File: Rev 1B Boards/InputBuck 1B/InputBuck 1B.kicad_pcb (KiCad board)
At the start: 4 copper layers, 67.2 x 46 mm, 44 parts, among them J1 Conn_01x02_Socket, J16 Banana 2P, J17 Banana 2P, J23 Conn_01x01_Pin, Q1 BSC059N04LS6, Q2 BSC059N04LS6, U1 BQ24640

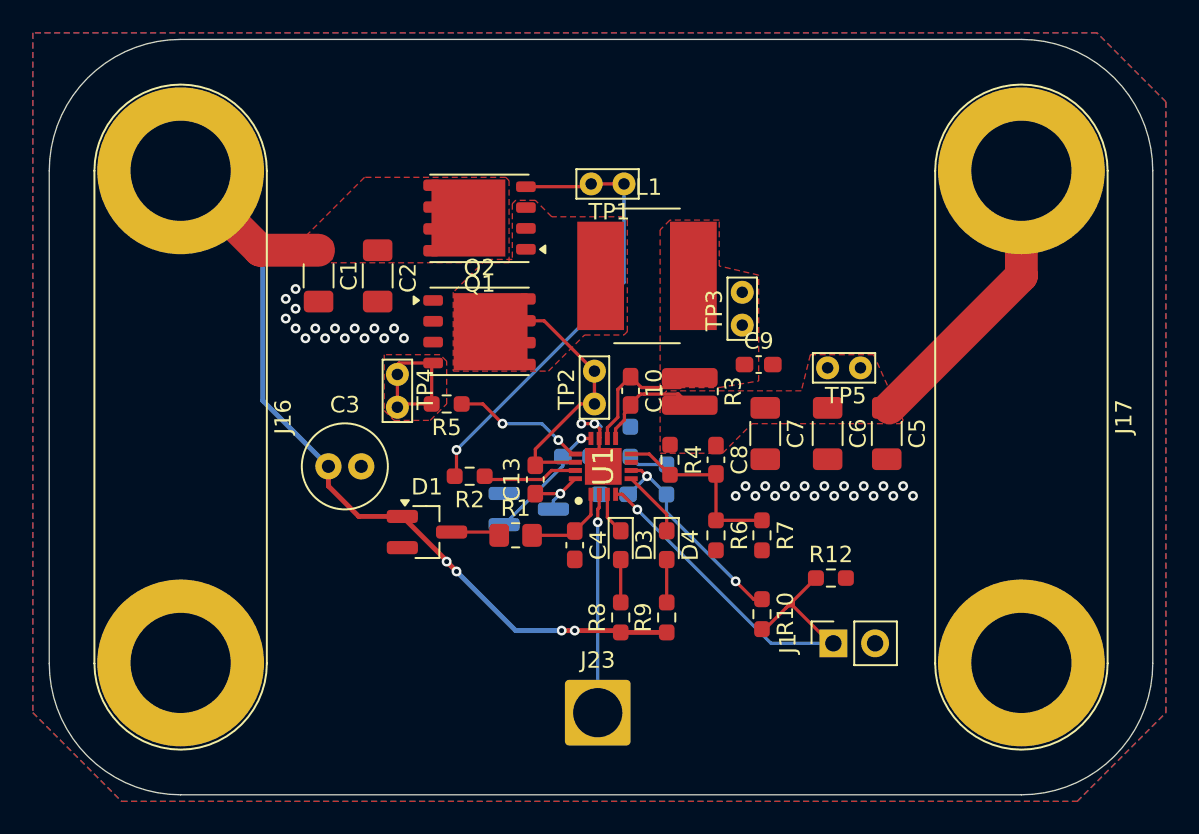
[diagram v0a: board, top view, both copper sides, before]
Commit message: Add thermistor to BOM
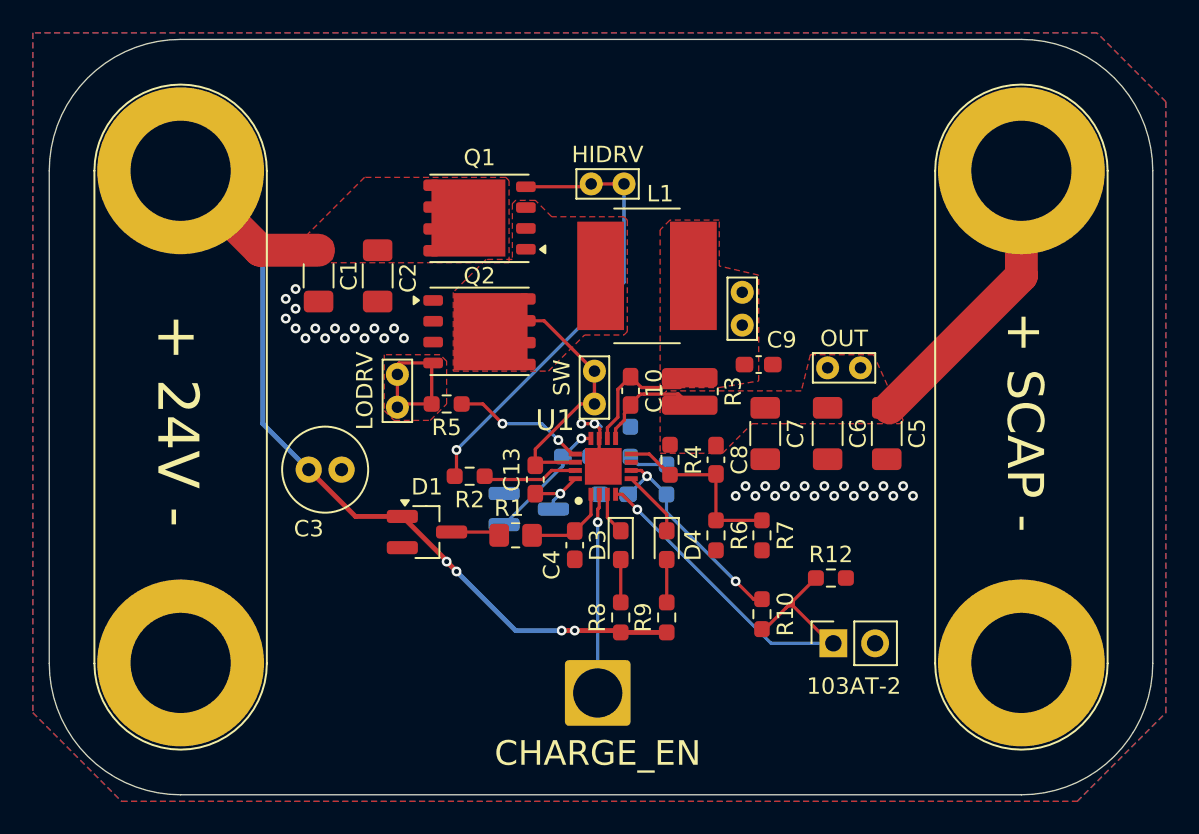
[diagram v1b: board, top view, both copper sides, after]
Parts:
- moved C3 1.22 mm to (104.6, 137.8)
- moved J23 1.20 mm to (122.2, 151.4)
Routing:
- net /CHARGE_EN_IN: track 13.3 -> 12.1 mm
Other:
- board text added: "+ 24V -"
- board text added: "+ SCAP -"
- board text added: "103AT-2"
- board text added: "CHARGE_EN"
- board text added: "HIDRV"
- board text added: "LODRV"
- board text added: "OUT"
- board text added: "SW"
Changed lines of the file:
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@@
 		(tags "LED handsolder")
 		(property "Reference" "D3"
-			(at 0 -1.43 90)
+			(at 0 1.4 90)
 			(layer "F.SilkS")
 			(effects
@@
 			(at 1.1 1.7 0)
 			(layer "F.SilkS")
+			(hide yes)
 			(effects
 				(font
@@
 		(tags "Infineon OptiMOS")
 		(property "Reference" "Q1"
-			(at 0 -4.025 0)
+			(at 0 3.675 0)
 			(layer "F.SilkS")
 			(effects
@@
 			(at 1.1 1.7 90)
 			(layer "F.SilkS")
+			(hide yes)
 			(effects
 				(font
@@
 			(at 1.1 1.7 90)
 			(layer "F.SilkS")
+			(hide yes)
 			(effects
 				(font
@@
 		(tags "capacitor handsolder")
 		(property "Reference" "C13"
-			(at 0 -1.43 90)
+			(at 0.6 -1.43 90)
 			(layer "F.SilkS")
 			(effects
@@
 			(at 1.1 1.7 90)
 			(layer "F.SilkS")
+			(hide yes)
 			(effects
 				(font
@@
 		(tags "Inductor")
 		(property "Reference" "L1"
-			(at 0.1 -5.4 0)
+			(at 0.8 -5 0)
 			(layer "F.SilkS")
 			(effects
@@
 		(tags "Infineon OptiMOS")
 		(property "Reference" "Q2"
-			(at 0 -3.9 0)
+			(at -0.005 -3.4 0)
 			(layer "F.SilkS")
 			(effects
@@
 			(at 14.985 -6.24 90)
 			(layer "F.SilkS")
+			(hide yes)
 			(effects
 				(font
@@
 	(footprint "Connector_Wire:SolderWire-2.5sqmm_1x01_D2.4mm_OD3.6mm"
 		(layer "F.Cu")
-		(at 122.2 152.6)
+		(at 122.2 151.4)
 		(descr "Soldered wire connection, for a single 2.5 mm² wire, basic insulation, conductor diameter 2.4mm, outer diameter 3.6mm, size source Multi-Contact FLEXI-E 2.5 (https://ec.staubli.com/AcroFiles/Catalogues/TM_Cab-Main-11014119_(en)_hi.pdf), bend radius 3 times outer diameter, generated with kicad-footprint-generator")
 		(tags "connector wire 2.5sqmm")
@@
 			(at 0 -3.2 0)
 			(layer "F.SilkS")
+			(hide yes)
 			(effects
 				(font
@@
 			(at 1.1 1.7 180)
 			(layer "F.SilkS")
+			(hide yes)
 			(effects
 				(font
@@
 		(tags "Integrated Circuit")
 		(property "Reference" "U1"
-			(at 0 0 90)
+			(at 2.8 -2.9375 180)
 			(layer "F.SilkS")
 			(effects
@@
 			)
 		)
+		(model "${KIPRJMOD}/../../KiCad_Library/ICs.3dmodels/BQ24640RVAR.stp"
+			(offset
+				(xyz 0 0 0)
+			)
+			(scale
+				(xyz 1 1 1)
+			)
+			(rotate
+				(xyz 0 0 0)
+			)
+		)
 	)
 	(footprint "Capacitor_SMD:C_0603_1608Metric_Pad1.08x0.95mm_HandSolder"
@@
 		(tags "capacitor handsolder")
 		(property "Reference" "C9"
-			(at 0 -1.43 0)
+			(at 1.4 -1.5 0)
 			(layer "F.SilkS")
 			(effects
@@
 		(tags "resistor handsolder")
 		(property "Reference" "R1"
-			(at 0 -1.65 0)
+			(at -0.4 -1.65 0)
 			(layer "F.SilkS")
 			(effects
@@
 		(tags "capacitor handsolder")
 		(property "Reference" "C4"
-			(at 0 -1.43 90)
+			(at 1.2 1.4 90)
 			(layer "F.SilkS")
 			(effects
@@
 		(tags "LED handsolder")
 		(property "Reference" "D4"
-			(at 0 -1.43 90)
+			(at 0 -1.6 90)
 			(layer "F.SilkS")
 			(effects
@@
 			(at 0 -2.77 90)
 			(layer "F.SilkS")
+			(hide yes)
 			(effects
 				(font
@@
 	(footprint "Capacitor_THT:C_Radial_D5.0mm_H11.0mm_P2.00mm"
 		(layer "F.Cu")
-		(at 105.8 137.6)
+		(at 104.6 137.8)
 		(descr "C, Radial series, Radial, pin pitch=2.00mm, diameter=5mm, height=11mm, Non-Polar Electrolytic Capacitor")
 		(tags "C Radial series Radial pin pitch 2.00mm diameter 5mm height 11mm Non-Polar Electrolytic Capacitor")
 		(property "Reference" "C3"
-			(at 1 -3.75 0)
+			(at 0 3.6 0)
 			(layer "F.SilkS")
 			(effects
@@
 			(at 14.985 -6.24 90)
 			(layer "F.SilkS")
+			(hide yes)
 			(effects
 				(font
@@
 		(layer "User.1")
 	)
+	(gr_text "SW"
+		(at 120.6 132.2 90)
+		(layer "F.SilkS" knockout)
+		(effects
+			(font
+				(size 1 1)
+				(thickness 0.125)
+			)
+			(justify bottom)
+		)
+	)
+	(gr_text "103AT-2"
+		(at 137.8 150.4 0)
+		(layer "F.SilkS" knockout)
+		(effects
+			(font
+				(size 1 1)
+				(thickness 0.125)
+			)
+			(justify top)
+		)
+	)
+	(gr_text "HIDRV"
+		(at 122.8 119.2 0)
+		(layer "F.SilkS" knockout)
+		(effects
+			(font
+				(size 1 1)
+				(thickness 0.125)
+			)
+			(justify bottom)
+		)
+	)
+	(gr_text "CHARGE_EN"
+		(at 122.2 154.2 0)
+		(layer "F.SilkS" knockout)
+		(effects
+			(font
+				(size 1.5 1.5)
+				(thickness 0.1875)
+			)
+			(justify top)
+		)
+	)
+	(gr_text "OUT"
+		(at 137.2 130.4 0)
+		(layer "F.SilkS" knockout)
+		(effects
+			(font
+				(size 1 1)
+				(thickness 0.125)
+			)
+			(justify bottom)
+		)
+	)
+	(gr_text "+ SCAP -"
+		(at 148.2 134.888748 270)
+		(layer "F.SilkS" knockout)
+		(effects
+			(font
+				(size 2.2 2.2)
+				(thickness 0.275)
+			)
+		)
+	)
+	(gr_text "+ 24V -"
+		(at 96.6 134.8 270)
+		(layer "F.SilkS" knockout)
+		(effects
+			(font
+				(size 2.5 2.5)
+				(thickness 0.3125)
+			)
+		)
+	)
+	(gr_text "LODRV"
+		(at 108.6 133 90)
+		(layer "F.SilkS" knockout)
+		(effects
+			(font
+				(size 1 1)
+				(thickness 0.125)
+			)
+			(justify bottom)
+		)
+	)
 	(gr_text "UT Stampede\nSupercap Charger\nTest Board\n_{Kaitlyn Chang & Jed Wang}"
 		(at 154.6 133.2 0)
@@
 	)
 	(segment
-		(start 105.8 138.8)
-		(end 107.65 140.65)
+		(start 104.6 137.8)
+		(end 107.45 140.65)
 		(width 0.3)
 		(layer "F.Cu")
@@
 	)
 	(segment
-		(start 105.8 137.6)
-		(end 105.8 138.8)
-		(width 0.3)
-		(layer "F.Cu")
-		(net 2)
-	)
-	(segment
 		(start 123.6 147.7125)
 		(end 126.4 147.7125)
@@
 	)
 	(segment
-		(start 107.65 140.65)
-		(end 110.3 140.65)
-		(width 0.3)
-		(layer "F.Cu")
-		(net 2)
-	)
-	(segment
 		(start 101.6375 124.4375)
 		(end 96.8 119.6)
@@
 	)
 	(segment
+		(start 107.45 140.65)
+		(end 110.3 140.65)
+		(width 0.3)
+		(layer "F.Cu")
+		(net 2)
+	)
+	(segment
 		(start 110.3 140.65)
 		(end 113 143.35)
@@
 	)
 	(segment
-		(start 117.2 147.6)
-		(end 120 147.6)
+		(start 101.8 135)
+		(end 101.8 124.6)
 		(width 0.3)
 		(layer "B.Cu")
@@
 	)
 	(segment
-		(start 105.8 137.6)
-		(end 101.8 133.6)
+		(start 117.2 147.6)
+		(end 120 147.6)
 		(width 0.3)
 		(layer "B.Cu")
@@
 	)
 	(segment
-		(start 101.8 133.6)
-		(end 101.8 124.6)
+		(start 104.6 137.8)
+		(end 101.8 135)
 		(width 0.3)
 		(layer "B.Cu")
@@
 	)
 	(segment
-		(start 113.6 144)
-		(end 117.2 147.6)
+		(start 101.8 124.6)
+		(end 96.8 119.6)
 		(width 0.3)
 		(layer "B.Cu")
@@
 	)
 	(segment
-		(start 101.8 124.6)
-		(end 96.8 119.6)
+		(start 113.6 144)
+		(end 117.2 147.6)
 		(width 0.3)
 		(layer "B.Cu")
@@
 	)
 	(segment
-		(start 122.2 152.6)
+		(start 122.2 151.4)
 		(end 122.2 141)
 		(width 0.2)

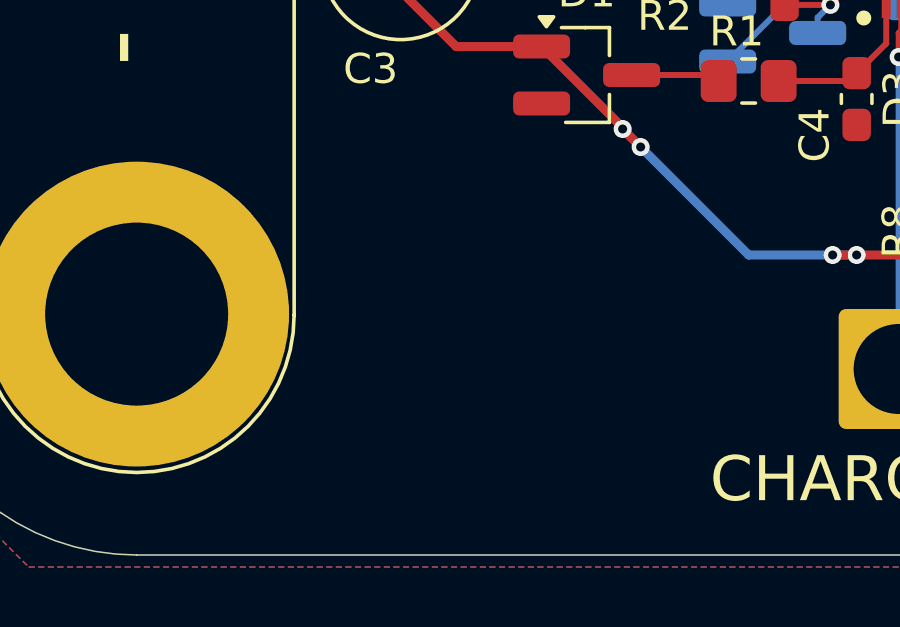
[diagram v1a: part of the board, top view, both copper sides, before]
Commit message: Polish input buck test board
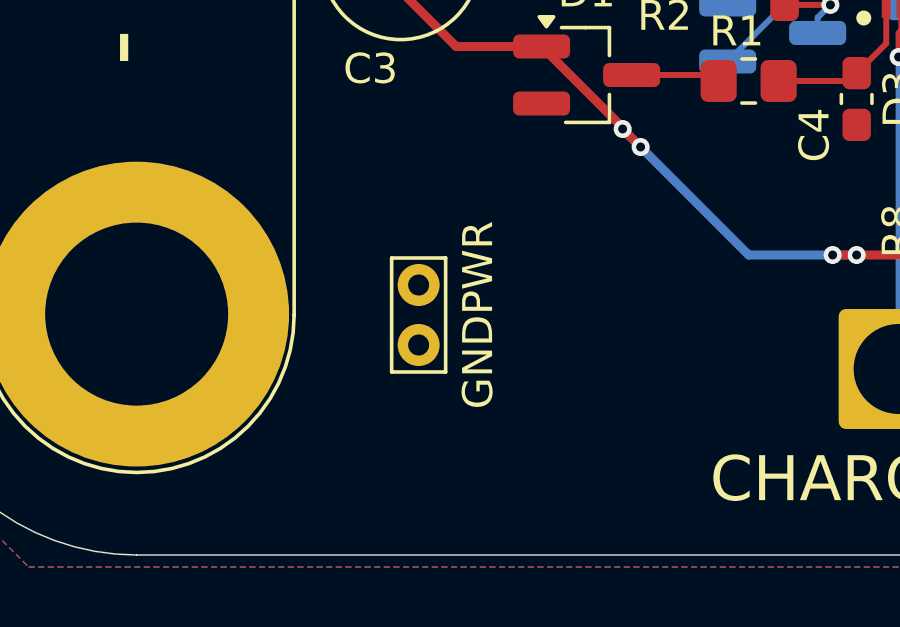
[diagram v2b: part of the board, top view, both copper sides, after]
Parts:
- added TP6: V_{LODRV}, TestPoint:TestPoint_Bridge_Pitch2.0mm_Drill0.7mm, F.Cu at (106.2, 150.6)
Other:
- board text added: "GNDPWR"

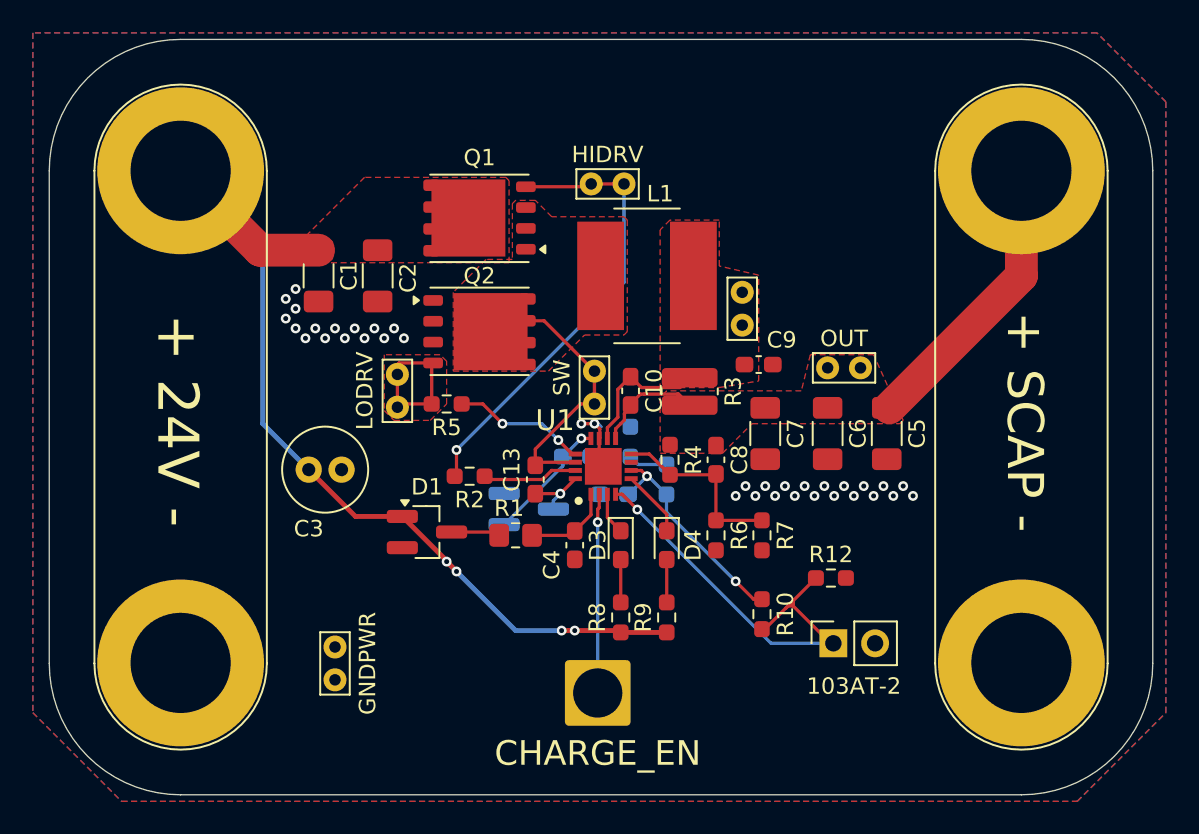
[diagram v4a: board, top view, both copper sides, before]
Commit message: Replace most banana jacks with XT connectors
+ update library
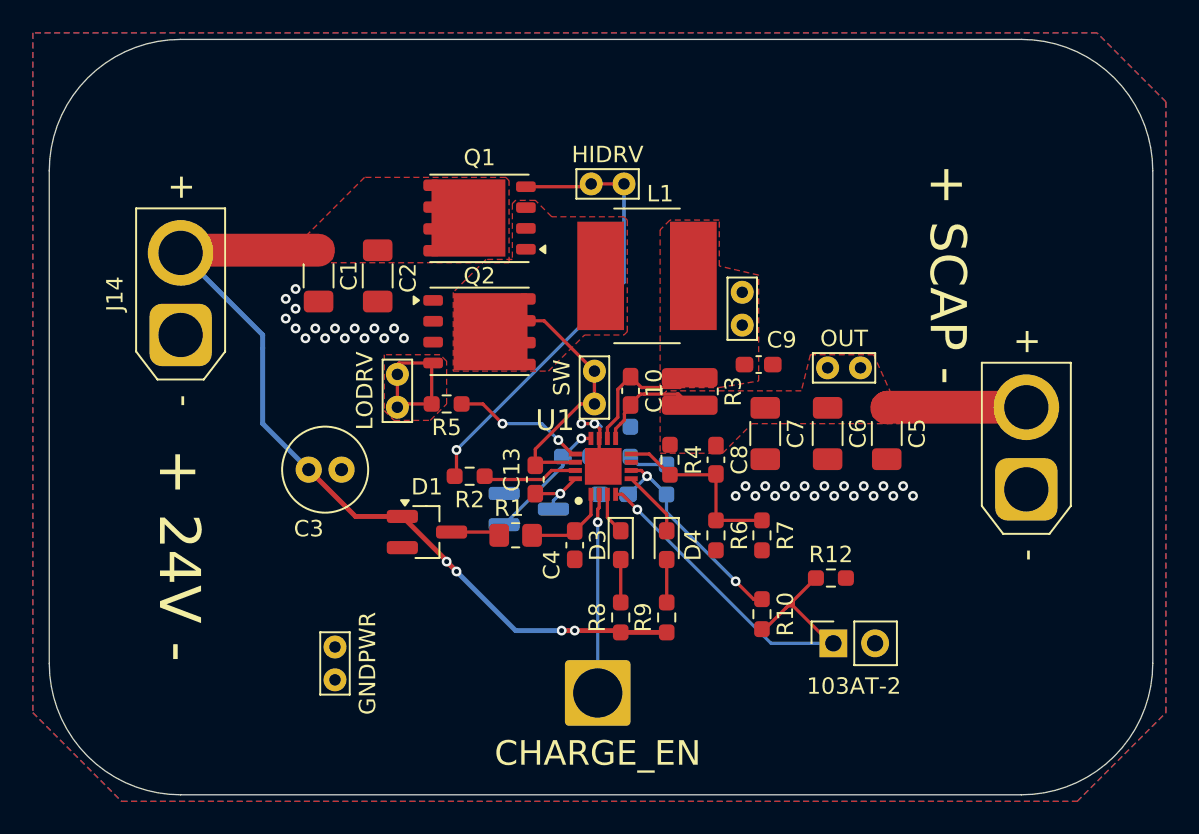
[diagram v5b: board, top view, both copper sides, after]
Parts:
- removed J16, J17: Banana 2P, Connector:Banana_Jack_2Pin
- added J14: XT30_F, Connector_AMASS:AMASS_XT30U-F_1x02_P5.0mm_Vertical, F.Cu at (96.8, 129.6)
- added J15: XT30_F, Connector_AMASS:AMASS_XT30U-F_1x02_P5.0mm_Vertical, F.Cu at (148.3, 139.0)
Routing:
- net /+6V_{SCAP}_OUT: track 24.5 -> 15.3 mm
- net /+24_IN: track 59.4 -> 52.5 mm
